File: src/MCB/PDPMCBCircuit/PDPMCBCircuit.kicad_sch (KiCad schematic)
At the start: 64 parts

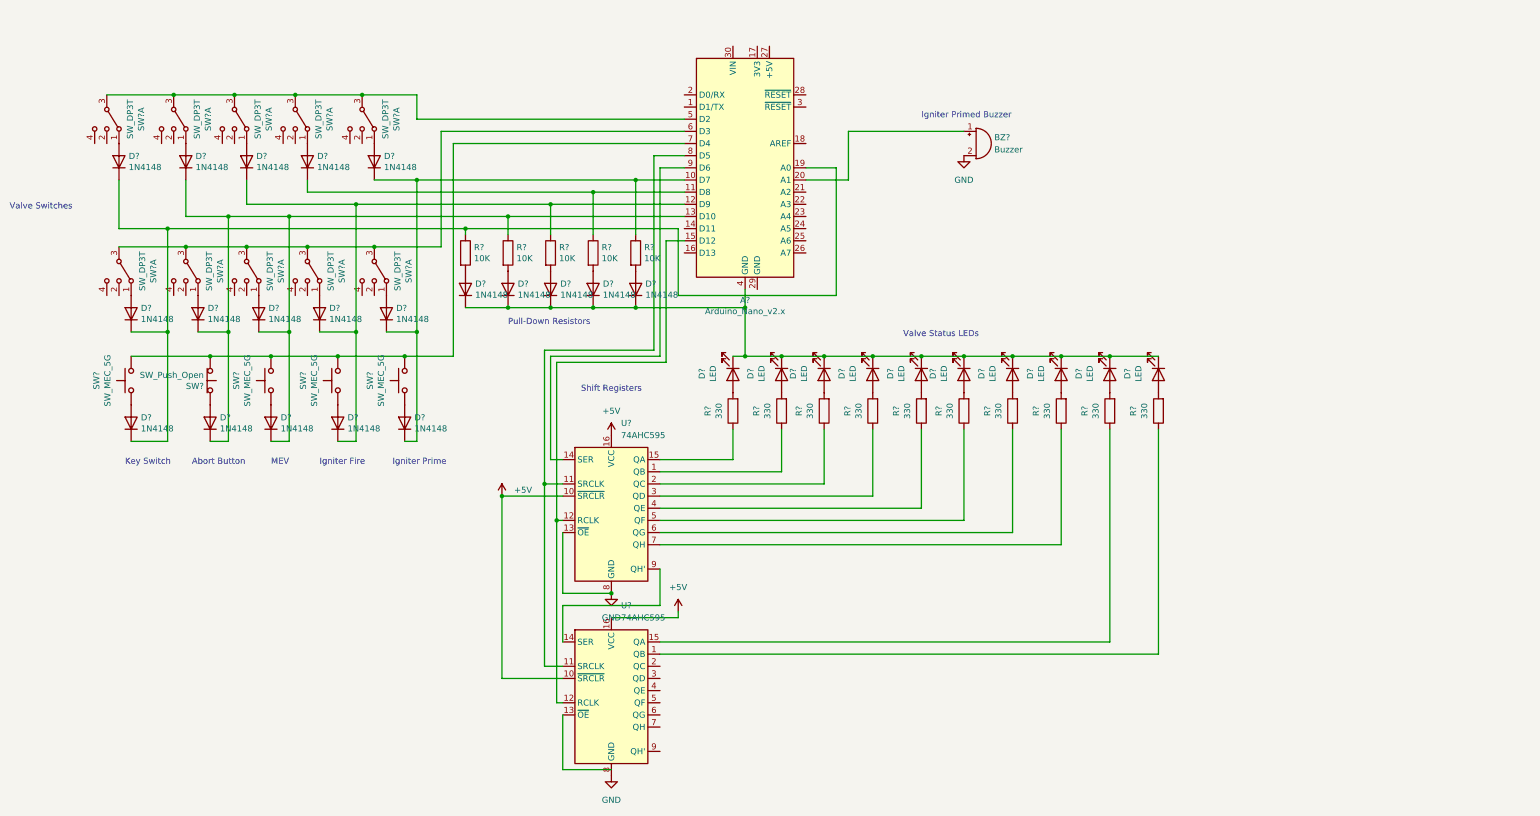
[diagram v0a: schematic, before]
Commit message: Started new design for MCB electrical
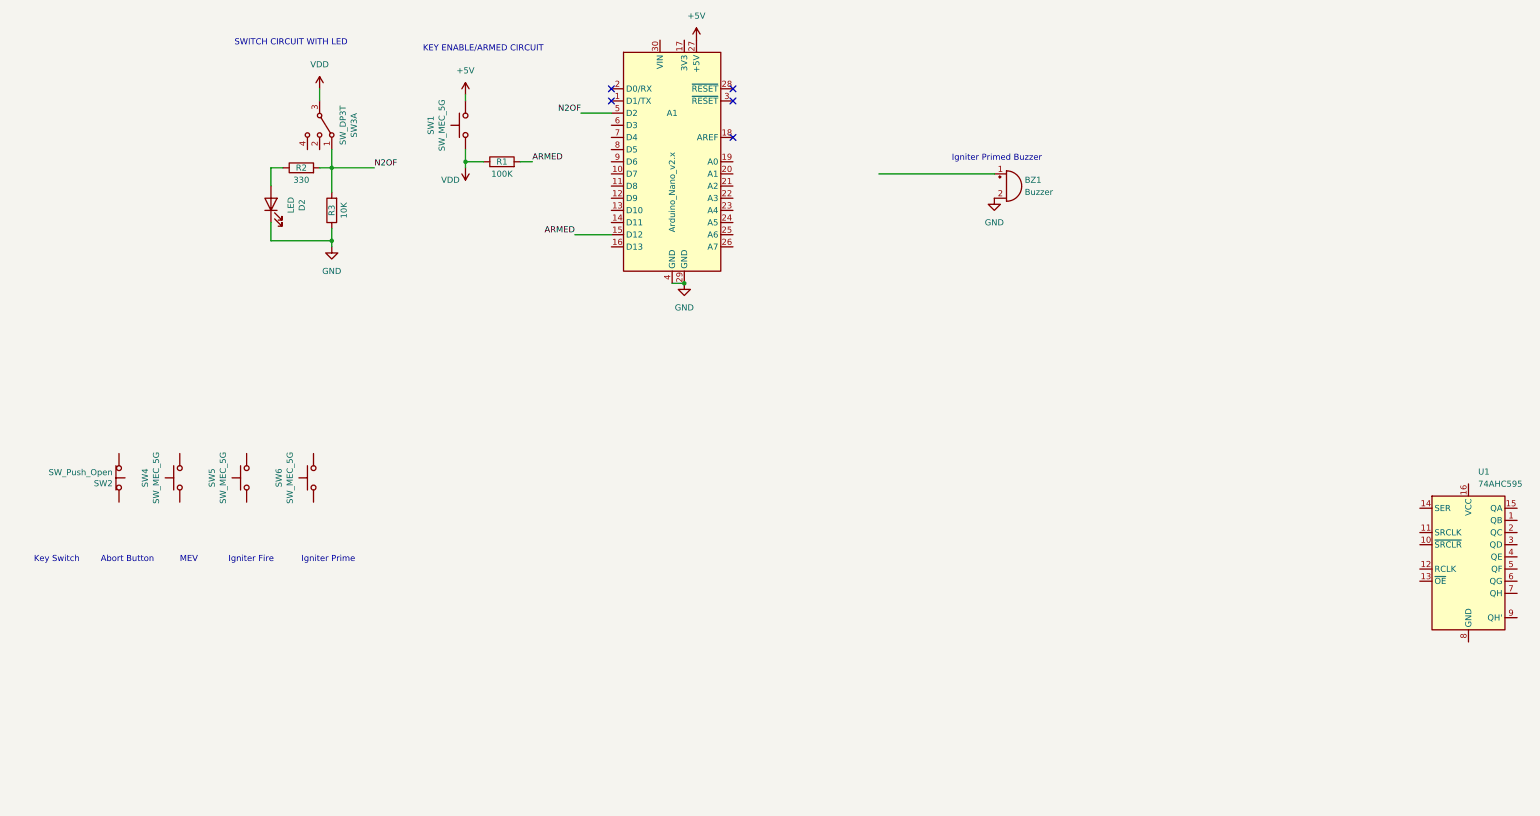
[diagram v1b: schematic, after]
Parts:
- removed D? (x20): 1N4148, Diode_THT:D_DO-35_SOD27_P7.62mm_Horizontal, symbol Diode:1N4148
- removed D? (x10): LED, symbol Device:LED
- removed R? (x5): 10K, symbol Device:R
- removed R? (x10): 330, symbol Device:R
- removed SW? (x10): SW_DP3T, symbol Switch:SW_DP3T
- removed U? (x2): 74AHC595, symbol 74xx:74AHC595
- added D2: LED, symbol Device:LED
- added R1: 100K, symbol Device:R
- added R2: 330, symbol Device:R
- added R3: 10K, symbol Device:R
- added SW3: SW_DP3T, symbol Switch:SW_DP3T
- added U1: 74AHC595, symbol 74xx:74AHC595
- gave numbers to parts that had none: 7
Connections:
- net +5V: now also A1.27 (+5V), SW1.3 (B), SW1.4 (B)
- net GND: now also A1.29 (GND), A1.4 (GND), D2.1 (K), R3.1
- net ARMED: now reaches A1.15 (D12)
- net ARMED: now also R1.2
- net at A1.20 (A1): no longer BZ1.1 (-)
- net N2OF: now reaches A1.5 (D2)
- net N2OF: now also R2.2, R3.2, SW3.1
- net VDD: now reaches SW1.1 (A), SW1.2 (A)
- net VDD: now also R1.1, SW3.3
- new net: SW4.3 (B), SW4.4 (B)
- new net: SW5.3 (B), SW5.4 (B)
- new net: SW6.3 (B), SW6.4 (B)
- new net: D2.2 (A), R2.1
- now unconnected: A1.7 (D4), SW2.1 (A)
- no-connect marks 0 -> 5
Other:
- note added: "KEY ENABLE/ARMED CIRCUIT"
- note added: "SWITCH CIRCUIT WITH LED"
- note removed: "Pull-Down Resistors"
- note removed: "Shift Registers"
- note removed: "Valve Status LEDs"
- note removed: "Valve Switches"
- moved on the sheet: A1, BZ1, SW1, SW2, SW4, SW5, SW6

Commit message: Updated Firmware for MCB
Implemented an array of active low switches, an interrupt for ARMKEY, and interrupt for ABORT
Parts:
- added D1, D3, D4, D5, D6, D7, D8, D9: LED, symbol Device:LED
- added R10, R11, R15, R16, R21, R22, R23, R6: 10K, symbol Device:R
- added R12, R17, R18, R19, R25, R7: 1K, symbol Device:R
- added R13, R14, R4, R5, R8, R9: 330, symbol Device:R
- added R20, R24: 100K, symbol Device:R
- added SW10, SW11, SW12, SW13, SW14, SW15, SW8, SW9: SW_DP3T, symbol Switch:SW_DP3T
- added SW16, SW7: SW_MEC_5G, symbol Switch:SW_MEC_5G
- R2: value 330 -> 100K
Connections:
- net +5V: now also SW1.1 (A), SW1.2 (A), R10.2, R13.2, R15.2, R4.2, R6.2, R8.2, SW16.1 (A), SW16.2 (A); no longer SW1.3 (B), SW1.4 (B)
- net ARMED: now also R1.1, R2.1, SW1.3 (B), SW1.4 (B), SW3.3, R24.1, R25.1, SW10.3, SW12.3, SW16.3 (B), SW16.4 (B); no longer A1.15 (D12), R1.2
- net GND: now also R1.2, R11.1, R14.1, R16.1, R20.2, R21.2, R22.2, R23.2, R24.2, R5.1, R9.1, SW7.1 (A), SW7.2 (A); no longer D2.1 (K)
- net N2OF: now also D1.1 (K), R12.1, R17.1, R6.1, R7.1, SW8.3; no longer A1.5 (D2), R2.2, R3.2, SW3.1
- net at D2.2 (A): now also R3.2, SW3.1, R7.2; no longer R2.1
- removed net VDD: R1.1, SW1.1 (A), SW1.2 (A), SW3.3
- new net: R2.2, SW11.1, SW7.3 (B), SW7.4 (B), SW8.1, SW9.1
- new net: D2.1 (K), R5.2
- new net: D4.2 (A), R11.2, R12.2, SW10.1
- new net: D7.1 (K), R21.1
- new net: D9.1 (K), R23.1
- new net: D3.2 (A), R8.1
- new net: D6.2 (A), R16.2, R17.2, SW12.1
- new net: D8.1 (K), R22.1
- new net: R18.1, R25.2, SW13.3
- new net: D1.2 (A), R4.1
- new net: R19.2, SW15.3
- new net: D4.1 (K), R9.2
- new net: R18.2, R19.1, SW14.3
- new net: D5.2 (A), R13.1
- new net: D6.1 (K), R14.2
- new net ADC Pin: R20.1, SW13.1, SW14.1, SW15.1
- new net GPIO_1: D7.2 (A)
- new net GPIO_2: D8.2 (A)
- new net GPIO_3: D9.2 (A)
- new net N2F: D5.1 (K), R15.1, SW11.3
- new net N2OV: D3.1 (K), R10.1, SW9.3
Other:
- note added: "*current already limited"
- note added: "*for current limiting input"
- note added: "ACTIVE HI SWITCHES"
- note added: "ACTIVE LO SWITCHES"
- note added: "ANALOG COMBINED SWITCHES"
- note added: "Arduino Nano Properties Max output DC current Vcc and GND pins = 200mA Max output each PORT = 150mA Max sink current each PORT = 100mA **from ATMEL328 Datasheet"
- note added: "MORE LEDS"
- note added: "MORE SWITCHES"
- note removed: "KEY ENABLE/ARMED CIRCUIT"
- note removed: "SWITCH CIRCUIT WITH LED"
- moved on the sheet: A1, BZ1, R1, R3, SW1, SW2, SW3A, SW4, SW5, SW6

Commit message: Finished electrical Schematic and Code to include all valves
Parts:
- removed R25: 1K, symbol Device:R
- removed SW10, SW12, SW13, SW14, SW15: SW_DP3T, symbol Switch:SW_DP3T
- removed SW16, SW4, SW5, SW6: SW_MEC_5G, symbol Switch:SW_MEC_5G
- removed SW2: SW_Push_Open, symbol Switch:SW_Push_Open
- removed U1: 74AHC595, symbol 74xx:74AHC595
- added D10, D11: LED, symbol Device:LED
- added SW10, SW12, SW13: SW_MEC_5G, symbol Switch:SW_MEC_5G
- added SW2, SW4, SW5, SW6: SW_DP3T, symbol Switch:SW_DP3T
- R1, R20: value 100K -> 330
- R12, R18: value 1K -> 330
- R14: value 330 -> 10K
- R16, R3: value 10K -> 330
- R17, R19, R7: value 1K -> 10K
- R24: value 100K -> 10K
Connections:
- net +5V: now also R1.2, R11.2, R12.2, R14.2, R16.2, R17.2, R18.2, R19.2, R2.1, R20.2, R21.2, R22.2, R23.2, R24.2, R3.2, R5.2, R7.2, R9.2; no longer SW1.1 (A), SW1.2 (A)
- net ARMED: now also A1.6 (D3), D2.1 (K), D4.1 (K), R2.2, SW11.1, SW3.1, SW7.3 (B), SW7.4 (B), SW8.1, SW9.1, SW10.3 (B), SW10.4 (B), SW12.3 (B), SW12.4 (B), SW13.3 (B), SW13.4 (B), SW2.1, SW4.1, SW5.1, SW6.1; no longer R1.1, R2.1, R24.1, SW1.3 (B), SW1.4 (B), SW3.3
- net GND: now also SW1.3 (B), SW1.4 (B); no longer R1.2, R11.1, R14.1, R16.1, R20.2, R21.2, R22.2, R23.2, R24.2, R3.1, R5.1, R9.1
- net N2F: now also A1.22 (A3)
- net N2OF: now also A1.24 (A5), D6.1 (K); no longer R12.1, R17.1, R7.1
- net N2OV: now also A1.23 (A4)
- net S1: now reaches A1.10 (D7)
- net S1: now also R19.1, D10.1 (K), SW5.3
- net S2: now reaches A1.11 (D8)
- net S2: now also R21.1, D11.1 (K), SW6.3
- net at A1.14 (D11): now also BZ1.1 (-)
- net EVV: now reaches A1.19 (A0)
- net EVV: now also D9.1 (K), R17.1, SW4.3
- net NCV: now reaches A1.20 (A1)
- net NCV: now also D8.1 (K), R14.1, SW3.3
- net RTV: now reaches A1.21 (A2)
- net RTV: now also D7.1 (K), R11.1, SW2.3
- net ABORT: now reaches A1.5 (D2)
- net ABORT: now also R7.1, SW1.1 (A), SW1.2 (A)
- net IGFIRE: now reaches A1.7 (D4)
- net IGFIRE: now also R23.1, SW12.1 (A), SW12.2 (A)
- net IGPRIME: now reaches A1.8 (D5)
- net IGPRIME: now also R22.1, SW10.1 (A), SW10.2 (A)
- net MEV: now reaches A1.9 (D6)
- net MEV: now also R24.1, SW13.1 (A), SW13.2 (A)
- net at R18.1: now also D10.2 (A)
- net at D1.2 (A), R4.1: now also D6.2 (A), R5.1
- net ADC Pin: no longer names the net of R20.1
- net ADC Pin: now also D11.2 (A)
- net GPIO_1: no longer names the net of D7.2 (A)
- net GPIO_1: now also R9.1
- net GPIO_2: no longer names the net of D8.2 (A)
- net GPIO_2: now also R12.1
- net GPIO_3: no longer names the net of D9.2 (A)
- net GPIO_3: now also R16.1
- new net: D2.2 (A), D4.2 (A), R1.1, R3.1
- no-connect marks 5 -> 29
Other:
- note removed: "*current already limited"
- note removed: "*for current limiting input"
- note removed: "ACTIVE HI SWITCHES"
- note removed: "ANALOG COMBINED SWITCHES"
- note removed: "Abort Button"
- note removed: "Igniter Fire"
- note removed: "Igniter Prime"
- note removed: "Key Switch"
- note removed: "MEV"
- note removed: "MORE LEDS"
- note removed: "MORE SWITCHES"
- moved on the sheet: A1, BZ1, D1, D3, D5, R10, R13, R15, R2, R4, R6, R8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

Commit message: Working Version
Finished a working version of the code
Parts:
- added R25: 100K, symbol Device:R
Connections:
- net GND: now also R25.2; no longer BZ1.2 (+)
- new net: BZ1.2 (+), R25.1
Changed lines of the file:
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@@
+    (stroke (width 0) (type default) (color 0 0 0 0))
+  )
+  (wire (pts (xy 90.17 127) (xy 90.17 128.27))
     (stroke (width 0) (type default) (color 0 0 0 0))
   )
@@
     (stroke (width 0) (type default) (color 0 0 0 0))
   )
-  (wire (pts (xy 90.17 127) (xy 90.17 129.54))
-    (stroke (width 0) (type default) (color 0 0 0 0))
-  )
   (wire (pts (xy 255.27 67.31) (xy 255.27 73.66))
     (stroke (width 0) (type default) (color 0 0 0 0))
@@
   )
   (wire (pts (xy 207.01 59.69) (xy 215.9 59.69))
+    (stroke (width 0) (type default) (color 0 0 0 0))
+  )
+  (wire (pts (xy 90.17 135.89) (xy 90.17 138.43))
     (stroke (width 0) (type default) (color 0 0 0 0))
   )
@@
     (pin "2")
   )
+  (symbol (lib_id "Device:R") (at 90.17 132.08 0) (unit 1)
+    (in_bom yes) (on_board yes)
+    (property "Reference" "R25" (id 0) (at 90.17 132.08 90))
+    (property "Value" "100K" (id 1) (at 92.71 132.08 90))
+    (property "Footprint" "" (id 2) (at 88.392 132.08 90)
+      (effects (font (size 1.27 1.27)) hide)
+    )
+    (property "Datasheet" "~" (id 3) (at 90.17 132.08 0)
+      (effects (font (size 1.27 1.27)) hide)
+    )
+    (pin "1")
+    (pin "2")
+  )
   (symbol (lib_id "power:+5V") (at 83.82 30.48 90) (unit 1)
     (in_bom yes) (on_board yes) (fields_autoplaced)
@@
     (pin "2")
   )
-  (symbol (lib_id "power:GND") (at 90.17 129.54 0) (unit 1)
+  (symbol (lib_id "power:GND") (at 90.17 138.43 0) (unit 1)
     (in_bom yes) (on_board yes) (fields_autoplaced)
-    (property "Reference" "#PWR03" (id 0) (at 90.17 135.89 0)
-      (effects (font (size 1.27 1.27)) hide)
-    )
-    (property "Value" "GND" (id 1) (at 90.17 134.62 0))
-    (property "Footprint" "" (id 2) (at 90.17 129.54 0)
-      (effects (font (size 1.27 1.27)) hide)
-    )
-    (property "Datasheet" "" (id 3) (at 90.17 129.54 0)
+    (property "Reference" "#PWR03" (id 0) (at 90.17 144.78 0)
+      (effects (font (size 1.27 1.27)) hide)
+    )
+    (property "Value" "GND" (id 1) (at 90.17 143.51 0))
+    (property "Footprint" "" (id 2) (at 90.17 138.43 0)
+      (effects (font (size 1.27 1.27)) hide)
+    )
+    (property "Datasheet" "" (id 3) (at 90.17 138.43 0)
       (effects (font (size 1.27 1.27)) hide)
     )
@@
       (reference "R24") (unit 1) (value "10K") (footprint "")
     )
+    (path "/1d15ae4f-3a41-4306-b521-491cc5c9a507"
+      (reference "R25") (unit 1) (value "100K") (footprint "")
+    )
     (path "/500cd68b-c8e1-41aa-9a10-3e9ad6d7f993"

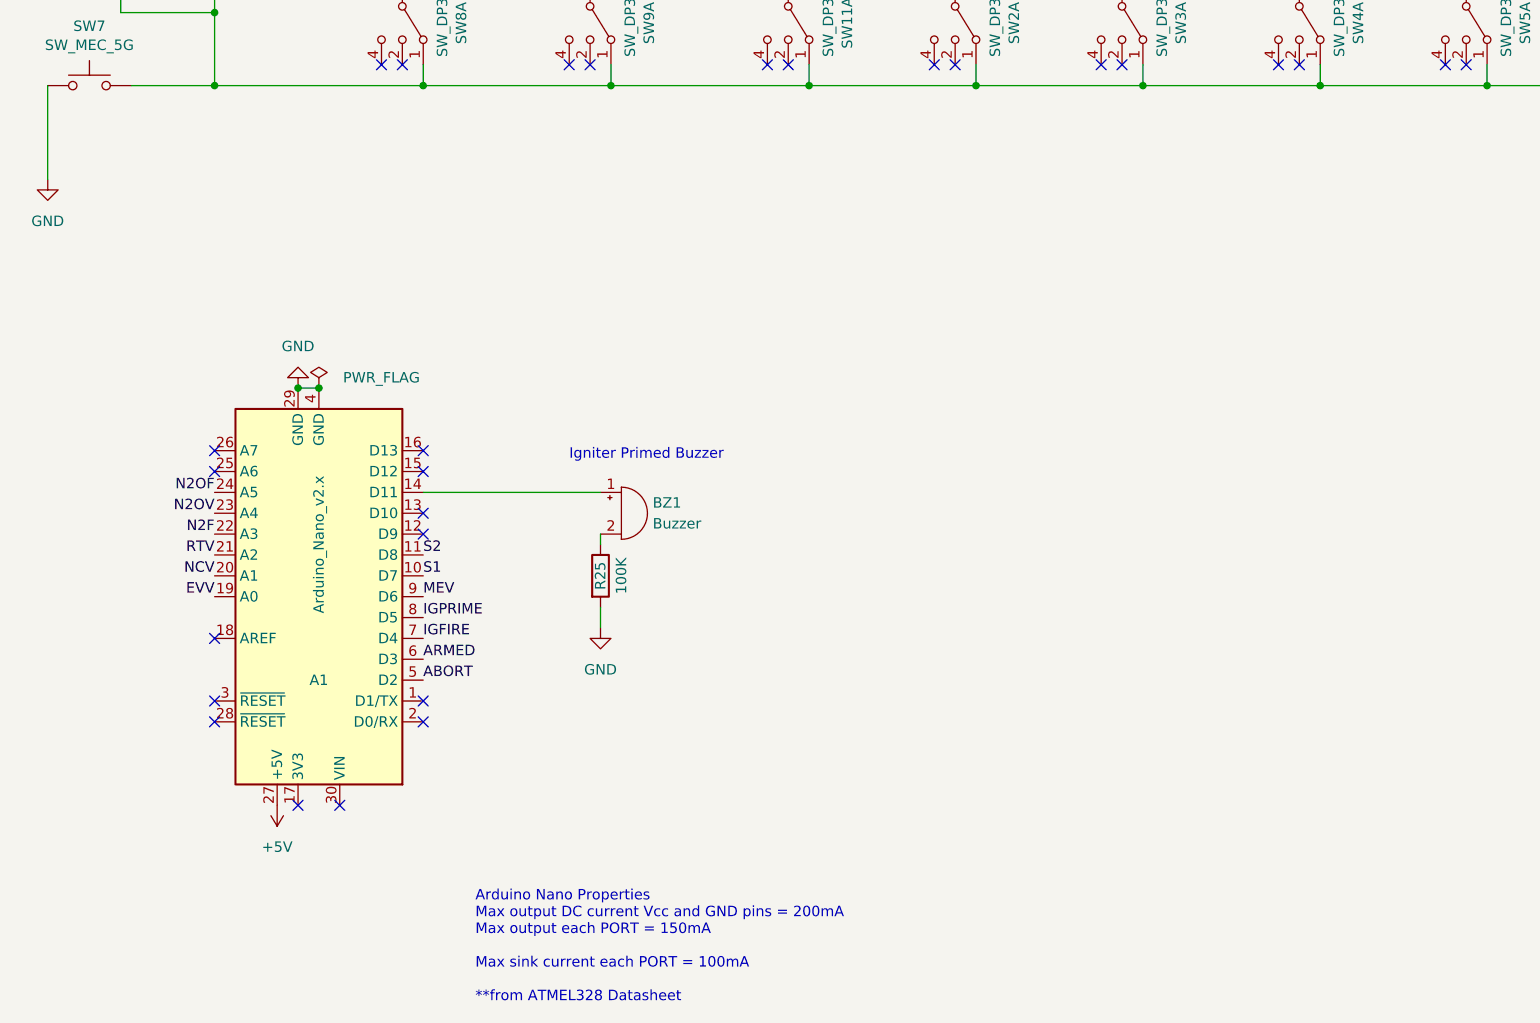
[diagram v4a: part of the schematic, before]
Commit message: Fixed abort and buzzer bugs
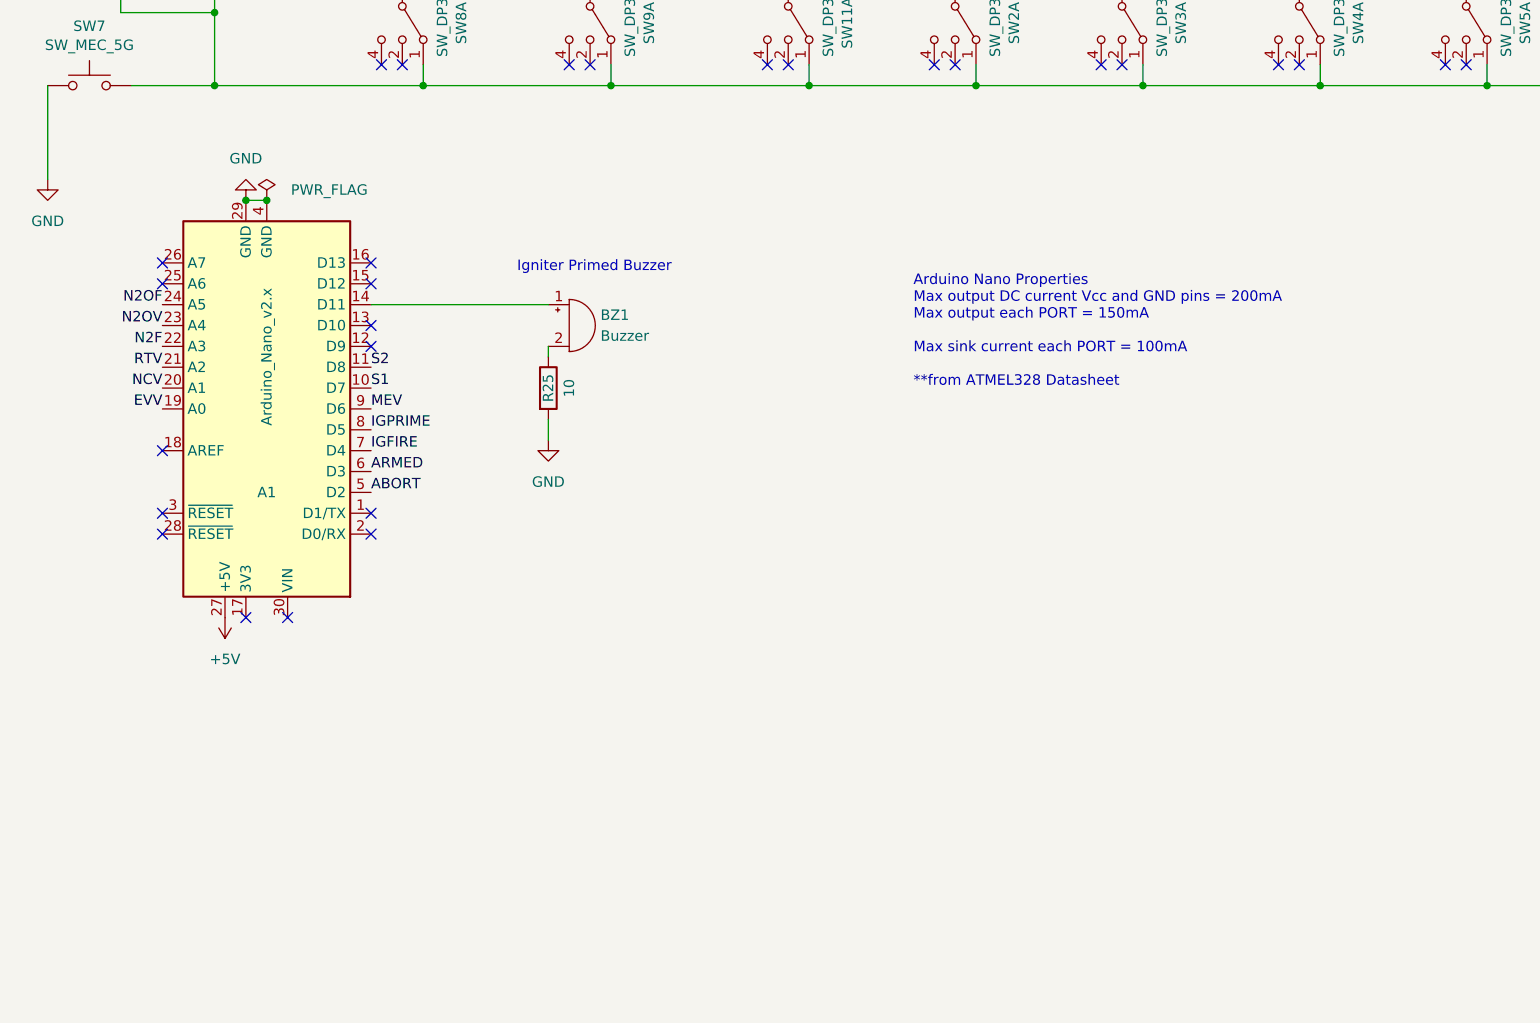
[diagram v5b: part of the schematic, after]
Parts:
- R25: value 100K -> 10
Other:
- moved on the sheet: A1, BZ1, R25
